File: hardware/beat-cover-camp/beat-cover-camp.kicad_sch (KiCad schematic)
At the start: 11 parts

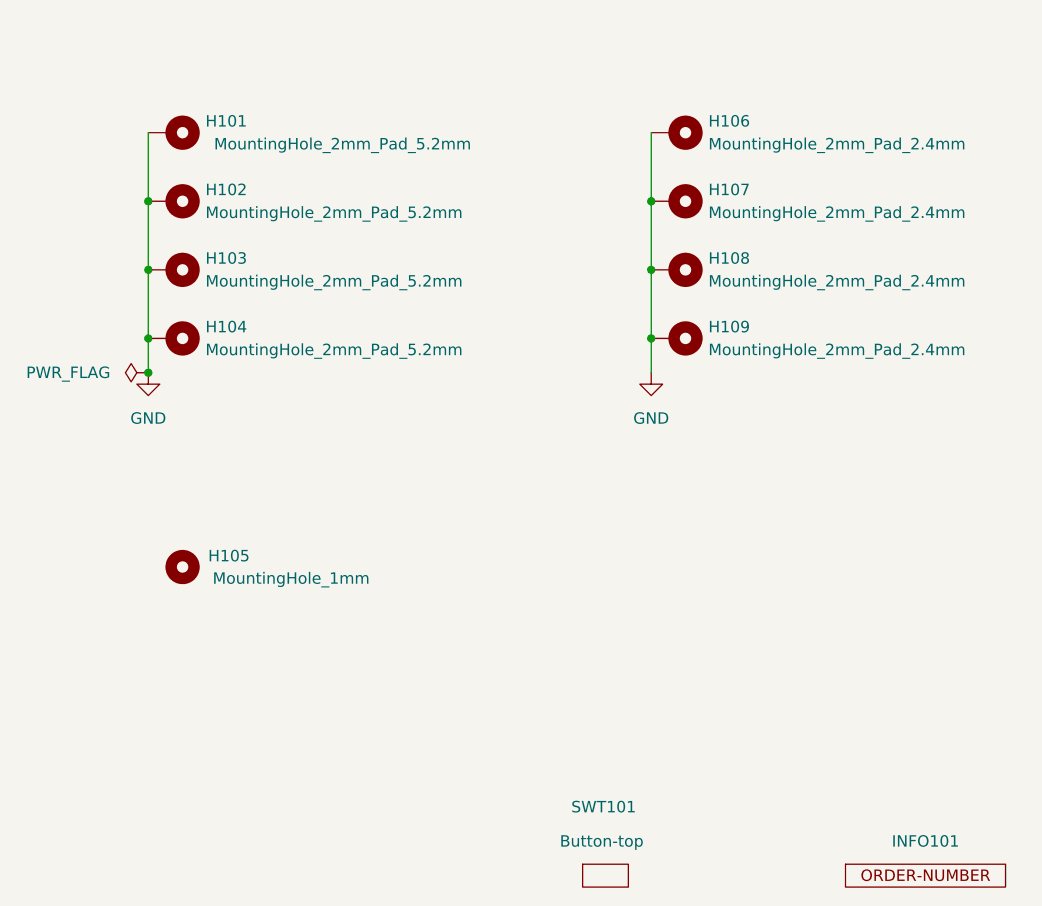
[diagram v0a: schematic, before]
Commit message: Replace Order_Number
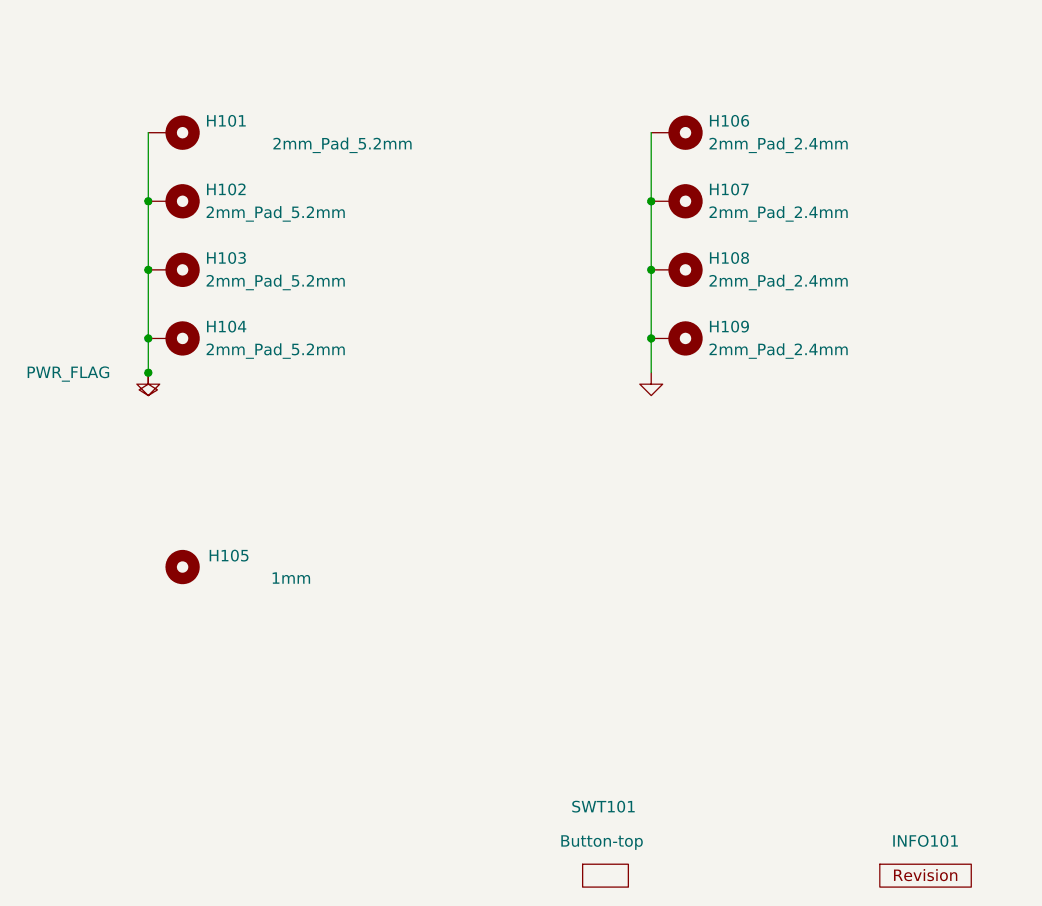
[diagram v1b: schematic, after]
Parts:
- H101, H102, H103, H104: value MountingHole_2mm_Pad_5.2mm -> 2mm_Pad_5.2mm; footprint V2_Mechanical:Mounting_Hole_2mm_Pad_5.2mm -> V2_Mechanical:MountingHole_2mm_Pad_5.2mm
- H105: value MountingHole_1mm -> 1mm
- H106, H107, H108, H109: value MountingHole_2mm_Pad_2.4mm -> 2mm_Pad_2.4mm
- INFO101: value ORDER-NUMBER -> ~; footprint V2_Production:Order_Number -> V2_Production:Revision; symbol V2_Production:Order_Number -> V2_Production:Revision
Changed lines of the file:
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@@
 (kicad_sch
-	(version 20231120)
+	(version 20250114)
 	(generator "eeschema")
-	(generator_version "8.0")
+	(generator_version "9.0")
 	(paper "A4")
 	(title_block
 		(title "V2 beat")
-		(date "2023-05-04")
-		(rev "0")
+		(date "2026-02-13")
+		(rev "2023-05-04")
 		(company "Versio Duo")
 		(comment 1 "Cover")
@@
 	)
 	(symbol
-		(lib_id "power:GND")
+		(lib_id "V2_power:GND")
 		(at 105.41 85.09 0)
 		(unit 1)
@@
 					(size 1.27 1.27)
 				)
+				(hide yes)
 			)
 		)
@@
 		(at 107.95 66.04 270)
 		(unit 1)
-		(exclude_from_sim yes)
+		(exclude_from_sim no)
 		(in_bom no)
 		(on_board yes)
@@
 			)
 		)
-		(property "Value" "MountingHole_2mm_Pad_5.2mm"
+		(property "Value" "2mm_Pad_5.2mm"
 			(at 111.76 67.3099 90)
 			(effects
@@
 			)
 		)
-		(property "Footprint" "V2_Mechanical:Mounting_Hole_2mm_Pad_5.2mm"
+		(property "Footprint" "V2_Mechanical:MountingHole_2mm_Pad_5.2mm"
 			(at 107.95 66.04 0)
 			(effects
@@
 			)
 		)
-		(property "Description" ""
+		(property "Description" "Mounting Hole with connection"
 			(at 107.95 66.04 0)
 			(effects
@@
 		(at 163.83 58.42 270)
 		(unit 1)
-		(exclude_from_sim yes)
+		(exclude_from_sim no)
 		(in_bom no)
 		(on_board yes)
@@
 			)
 		)
-		(property "Value" "MountingHole_2mm_Pad_2.4mm"
+		(property "Value" "2mm_Pad_2.4mm"
 			(at 167.64 59.6899 90)
 			(effects
@@
 			)
 		)
-		(property "Datasheet" "~"
+		(property "Datasheet" ""
 			(at 163.83 58.42 0)
 			(effects
@@
 			)
 		)
-		(property "Description" ""
+		(property "Description" "Mounting Hole with connection"
 			(at 163.83 58.42 0)
 			(effects
@@
 	)
 	(symbol
-		(lib_id "power:GND")
+		(lib_id "V2_power:GND")
 		(at 161.29 85.09 0)
 		(unit 1)
@@
 					(size 1.27 1.27)
 				)
+				(hide yes)
 			)
 		)
@@
 	)
 	(symbol
-		(lib_id "V2_Production:Order_Number")
+		(lib_id "V2_Production:Revision")
 		(at 191.77 140.97 0)
 		(unit 1)
-		(exclude_from_sim yes)
+		(exclude_from_sim no)
 		(in_bom no)
 		(on_board yes)
@@
 			)
 		)
-		(property "Value" "ORDER-NUMBER"
+		(property "Value" "~"
 			(at 191.77 143.51 0)
 			(effects
@@
 			)
 		)
-		(property "Footprint" "V2_Production:Order_Number"
+		(property "Footprint" "V2_Production:Revision"
 			(at 191.77 146.05 0)
 			(effects
@@
 		(at 163.83 73.66 270)
 		(unit 1)
-		(exclude_from_sim yes)
+		(exclude_from_sim no)
 		(in_bom no)
 		(on_board yes)
@@
 			)
 		)
-		(property "Value" "MountingHole_2mm_Pad_2.4mm"
+		(property "Value" "2mm_Pad_2.4mm"
 			(at 167.64 74.9299 90)
 			(effects
@@
 			)
 		)
-		(property "Datasheet" "~"
+		(property "Datasheet" ""
 			(at 163.83 73.66 0)
 			(effects
@@
 			)
 		)
-		(property "Description" ""
+		(property "Description" "Mounting Hole with connection"
 			(at 163.83 73.66 0)
 			(effects
@@
 		(at 156.21 140.97 0)
 		(unit 1)
-		(exclude_from_sim yes)
+		(exclude_from_sim no)
 		(in_bom no)
 		(on_board yes)
@@
 			)
 		)
+		(property "Sim.Enable" "0"
+			(at 156.21 140.97 0)
+			(effects
+				(font
+					(size 1.27 1.27)
+				)
+				(hide yes)
+			)
+		)
 		(instances
 			(project "beat-cover-camp"
@@
 		(at 107.95 81.28 270)
 		(unit 1)
-		(exclude_from_sim yes)
+		(exclude_from_sim no)
 		(in_bom no)
 		(on_board yes)
@@
 			)
 		)
-		(property "Value" "MountingHole_2mm_Pad_5.2mm"
+		(property "Value" "2mm_Pad_5.2mm"
 			(at 111.76 82.5499 90)
 			(effects
@@
 			)
 		)
-		(property "Footprint" "V2_Mechanical:Mounting_Hole_2mm_Pad_5.2mm"
+		(property "Footprint" "V2_Mechanical:MountingHole_2mm_Pad_5.2mm"
 			(at 107.95 81.28 0)
 			(effects
@@
 			)
 		)
-		(property "Description" ""
+		(property "Description" "Mounting Hole with connection"
 			(at 107.95 81.28 0)
 			(effects
@@
 		(at 163.83 81.28 270)
 		(unit 1)
-		(exclude_from_sim yes)
+		(exclude_from_sim no)
 		(in_bom no)
 		(on_board yes)
@@
 			)
 		)
-		(property "Value" "MountingHole_2mm_Pad_2.4mm"
+		(property "Value" "2mm_Pad_2.4mm"
 			(at 167.64 82.5499 90)
 			(effects
@@
 			)
 		)
-		(property "Datasheet" "~"
+		(property "Datasheet" ""
 			(at 163.83 81.28 0)
 			(effects
@@
 			)
 		)
-		(property "Description" ""
+		(property "Description" "Mounting Hole with connection"
 			(at 163.83 81.28 0)
 			(effects
@@
 		(at 107.95 58.42 270)
 		(unit 1)
-		(exclude_from_sim yes)
+		(exclude_from_sim no)
 		(in_bom no)
 		(on_board yes)
@@
 			)
 		)
-		(property "Value" "MountingHole_2mm_Pad_5.2mm"
+		(property "Value" "2mm_Pad_5.2mm"
 			(at 127 59.6899 90)
 			(effects
@@
 			)
 		)
-		(property "Footprint" "V2_Mechanical:Mounting_Hole_2mm_Pad_5.2mm"
+		(property "Footprint" "V2_Mechanical:MountingHole_2mm_Pad_5.2mm"
 			(at 107.95 58.42 0)
 			(effects
@@
 			)
 		)
-		(property "Description" ""
+		(property "Description" "Mounting Hole with connection"
 			(at 107.95 58.42 0)
 			(effects
@@
 		(at 163.83 66.04 270)
 		(unit 1)
-		(exclude_from_sim yes)
+		(exclude_from_sim no)
 		(in_bom no)
 		(on_board yes)
@@
 			)
 		)
-		(property "Value" "MountingHole_2mm_Pad_2.4mm"
+		(property "Value" "2mm_Pad_2.4mm"
 			(at 167.64 67.3099 90)
 			(effects
@@
 			)
 		)
-		(property "Datasheet" "~"
+		(property "Datasheet" ""
 			(at 163.83 66.04 0)
 			(effects
@@
 			)
 		)
-		(property "Description" ""
+		(property "Description" "Mounting Hole with connection"
 			(at 163.83 66.04 0)
 			(effects
@@
 	)
 	(symbol
-		(lib_id "power:PWR_FLAG")
+		(lib_id "V2_power:PWR_FLAG")
 		(at 105.41 85.09 90)
 		(unit 1)
@@
 			)
 		)
-		(property "Datasheet" "~"
+		(property "Datasheet" ""
 			(at 105.41 85.09 0)
 			(effects
@@
 			)
 		)
-		(property "Description" ""
+		(property "Description" "Special symbol for telling ERC where power comes from"
 			(at 105.41 85.09 0)
 			(effects
@@
 		(at 109.22 106.68 0)
 		(unit 1)
-		(exclude_from_sim yes)
+		(exclude_from_sim no)
 		(in_bom no)
 		(on_board yes)
@@
 			)
 		)
-		(property "Value" "MountingHole_1mm"
+		(property "Value" "1mm"
 			(at 121.285 107.95 0)
 			(effects
@@
 			)
 		)
-		(property "Description" ""
+		(property "Description" "Mounting Hole without connection"
 			(at 109.22 106.68 0)
 			(effects
@@
 		(at 107.95 73.66 270)
 		(unit 1)
-		(exclude_from_sim yes)
+		(exclude_from_sim no)
 		(in_bom no)
 		(on_board yes)
@@
 			)
 		)
-		(property "Value" "MountingHole_2mm_Pad_5.2mm"
+		(property "Value" "2mm_Pad_5.2mm"
 			(at 111.76 74.9299 90)
 			(effects
@@
 			)
 		)
-		(property "Footprint" "V2_Mechanical:Mounting_Hole_2mm_Pad_5.2mm"
+		(property "Footprint" "V2_Mechanical:MountingHole_2mm_Pad_5.2mm"
 			(at 107.95 73.66 0)
 			(effects
@@
 			)
 		)
-		(property "Description" ""
+		(property "Description" "Mounting Hole with connection"
 			(at 107.95 73.66 0)
 			(effects
@@
 		)
 	)
+	(embedded_fonts no)
 )

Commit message: Update Library
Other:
- moved on the sheet: H105
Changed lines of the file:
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@@
-	)
-	(junction
-		(at 105.41 85.09)
-		(diameter 0)
-		(color 0 0 0 0)
 	)
 	(junction
@@
 		(dnp no)
 		(fields_autoplaced yes)
-		(property "Reference" "#PWR0101"
+		(property "Reference" "#PWR101"
 			(at 105.41 91.44 0)
 			(effects
@@
 			(project "beat-cover-camp"
 				(path "/6c8448b4-b04d-47e1-934e-e40cbe27a7be"
-					(reference "#PWR0101")
+					(reference "#PWR101")
 					(unit 1)
 				)
@@
 		(dnp no)
 		(fields_autoplaced yes)
-		(property "Reference" "#PWR0102"
+		(property "Reference" "#PWR102"
 			(at 161.29 91.44 0)
 			(effects
@@
 			(project "beat-cover-camp"
 				(path "/6c8448b4-b04d-47e1-934e-e40cbe27a7be"
-					(reference "#PWR0102")
+					(reference "#PWR102")
 					(unit 1)
 				)
@@
 	)
 	(symbol
+		(lib_id "V2_power:GND")
+		(at 118.11 46.99 90)
+		(unit 1)
+		(exclude_from_sim no)
+		(in_bom yes)
+		(on_board yes)
+		(dnp no)
+		(fields_autoplaced yes)
+		(property "Reference" "#PWR0103"
+			(at 124.46 46.99 0)
+			(effects
+				(font
+					(size 1.27 1.27)
+				)
+				(hide yes)
+			)
+		)
+		(property "Value" "GND"
+			(at 123.19 46.99 0)
+			(effects
+				(font
+					(size 1.27 1.27)
+				)
+				(hide yes)
+			)
+		)
+		(property "Footprint" ""
+			(at 118.11 46.99 0)
+			(effects
+				(font
+					(size 1.27 1.27)
+				)
+				(hide yes)
+			)
+		)
+		(property "Datasheet" ""
+			(at 118.11 46.99 0)
+			(effects
+				(font
+					(size 1.27 1.27)
+				)
+				(hide yes)
+			)
+		)
+		(property "Description" ""
+			(at 118.11 46.99 0)
+			(effects
+				(font
+					(size 1.27 1.27)
+				)
+				(hide yes)
+			)
+		)
+		(pin "1"
+		)
+		(instances
+			(project "beat-cover-camp"
+				(path "/6c8448b4-b04d-47e1-934e-e40cbe27a7be"
+					(reference "#PWR0103")
+					(unit 1)
+				)
+			)
+		)
+	)
+	(symbol
 		(lib_id "V2_Mechanical:MountingHole_2mm_Pad_5.2mm")
 		(at 107.95 58.42 270)
@@
 		)
 		(property "Value" "2mm_Pad_5.2mm"
-			(at 127 59.6899 90)
+			(at 120.142 59.6899 90)
 			(effects
 				(font
@@
 	(symbol
 		(lib_id "V2_power:PWR_FLAG")
-		(at 105.41 85.09 90)
+		(at 118.11 46.99 0)
 		(unit 1)
 		(exclude_from_sim no)
@@
 		(on_board yes)
 		(dnp no)
-		(property "Reference" "#FLG0101"
-			(at 103.505 85.09 0)
+		(property "Reference" "#FLG101"
+			(at 118.11 45.085 0)
 			(effects
 				(font
@@
 		)
 		(property "Value" "PWR_FLAG"
-			(at 96.52 85.09 90)
+			(at 109.728 46.99 0)
 			(effects
 				(font
@@
 		)
 		(property "Footprint" ""
-			(at 105.41 85.09 0)
-			(effects
-				(font
-					(size 1.27 1.27)
-				)
-				(hide yes)
-			)
-		)
-		(property "Datasheet" ""
-			(at 105.41 85.09 0)
+			(at 118.11 46.99 0)
+			(effects
+				(font
+					(size 1.27 1.27)
+				)
+				(hide yes)
+			)
+		)
+		(property "Datasheet" ""
+			(at 118.11 46.99 0)
 			(effects
 				(font
@@
 		)
 		(property "Description" "Special symbol for telling ERC where power comes from"
-			(at 105.41 85.09 0)
-			(effects
-				(font
-					(size 1.27 1.27)
-				)
-				(hide yes)
-			)
-		)
-		(pin "1"
-		)
-		(instances
-			(project "beat-cover-camp"
-				(path "/6c8448b4-b04d-47e1-934e-e40cbe27a7be"
-					(reference "#FLG0101")
+			(at 118.11 46.99 0)
+			(effects
+				(font
+					(size 1.27 1.27)
+				)
+				(hide yes)
+			)
+		)
+		(pin "1"
+		)
+		(instances
+			(project "beat-cover-camp"
+				(path "/6c8448b4-b04d-47e1-934e-e40cbe27a7be"
+					(reference "#FLG101")
 					(unit 1)
 				)
@@
 	(symbol
 		(lib_id "V2_Mechanical:MountingHole_1mm")
-		(at 109.22 106.68 0)
+		(at 109.22 104.14 0)
 		(unit 1)
 		(exclude_from_sim no)
@@
 		(dnp no)
 		(property "Reference" "H105"
-			(at 112.0577 105.4569 0)
+			(at 112.0577 102.9169 0)
 			(effects
 				(font
@@
 		)
 		(property "Value" "1mm"
-			(at 121.285 107.95 0)
+			(at 114.427 105.664 0)
 			(effects
 				(font
@@
 		)
 		(property "Footprint" "V2_Mechanical:MountingHole_1mm"
-			(at 109.22 111.76 0)
-			(effects
-				(font
-					(size 1.27 1.27)
-				)
-				(hide yes)
-			)
-		)
-		(property "Datasheet" ""
-			(at 109.22 106.68 0)
+			(at 109.22 109.22 0)
+			(effects
+				(font
+					(size 1.27 1.27)
+				)
+				(hide yes)
+			)
+		)
+		(property "Datasheet" ""
+			(at 109.22 104.14 0)
 			(effects
 				(font
@@
 		)
 		(property "Description" "Mounting Hole without connection"
-			(at 109.22 106.68 0)
-			(effects
-				(font
+			(at 109.22 104.14 0)
+			(effects
+				(font
